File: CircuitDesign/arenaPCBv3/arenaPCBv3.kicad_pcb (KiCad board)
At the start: 2 copper layers, 86 x 67 mm, 29 parts, among them Q1 BSC007N04LS6

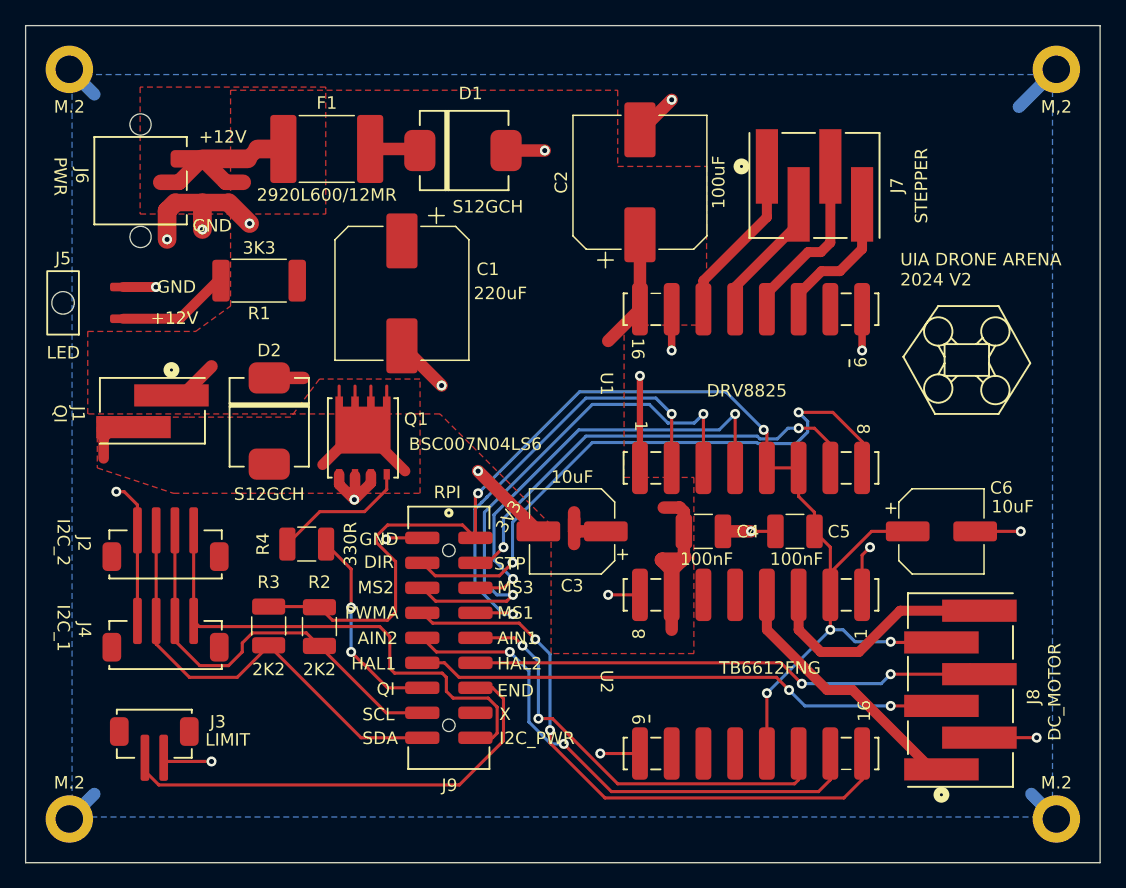
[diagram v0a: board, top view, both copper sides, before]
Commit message: new CAD parts for actuator
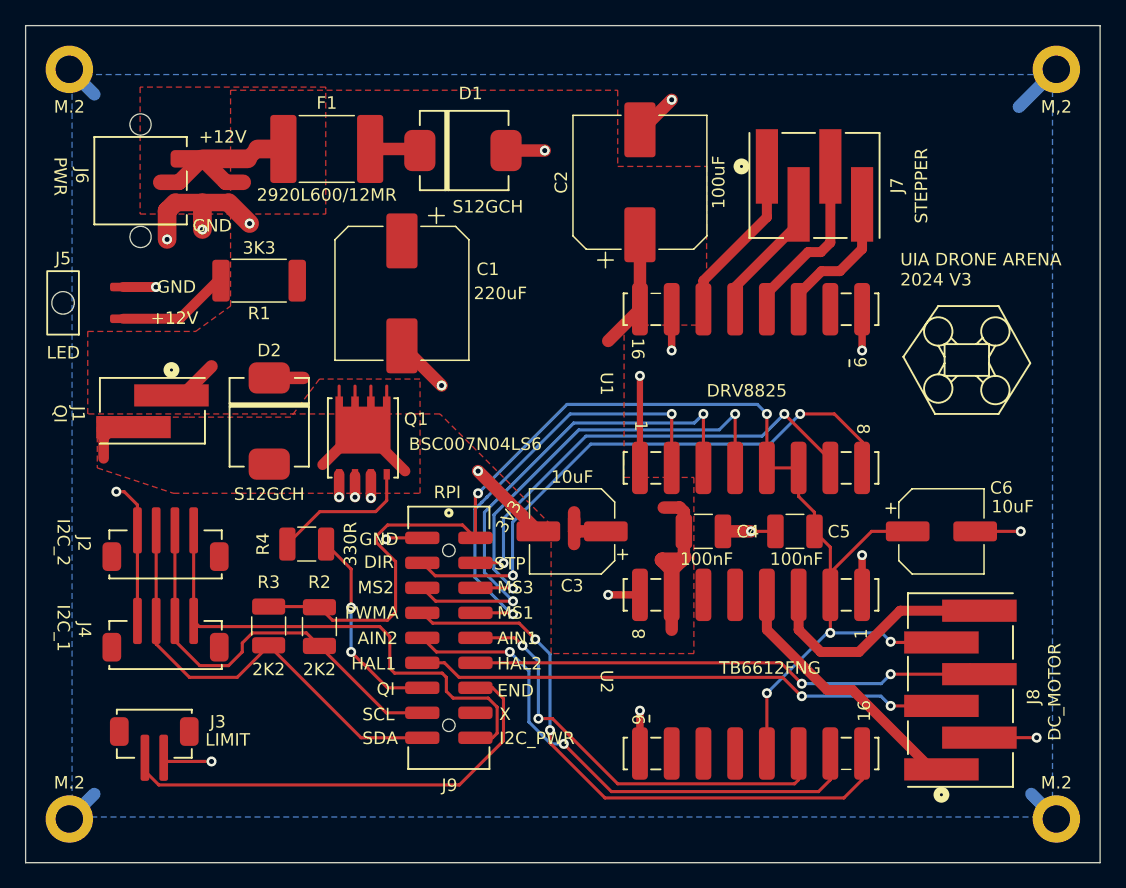
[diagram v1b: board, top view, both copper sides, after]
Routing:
- net GND: track 108.0 -> 105.9 mm, vias 21 -> 23
- net Net-(J9-MS2): track 42.6 -> 40.9 mm
- net Net-(J9-DIR): track 48.0 -> 46.5 mm
- net Net-(J9-MS1): track 37.4 -> 36.0 mm
- net Net-(J9-STEP): track 36.8 -> 37.6 mm
- net /G: track 11.0 -> 11.5 mm
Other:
- board text added: "UIA DRONE ARENA 2024 V3"
- board text removed: "UIA DRONE ARENA 2024 V2"
